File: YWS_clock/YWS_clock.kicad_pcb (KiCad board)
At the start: 2 copper layers, 140 x 90 mm, 63 parts, among them J1 Conn_01x06, J2 Power_inlet_vertical, J3 Conn_01x06, J4 Conn_02x03_Odd_Even, SW1 Omron_B3F_SPST, SW2 Omron_B3F_SPST, SW3 Omron_B3F_SPST, SW4 Omron_B3F_SPST, U1 L7805, U2 ATmega328-PU, U3 DS1307_DIP-8, U4 MAX7219, U5 MAX7219, U6 MAX7219, U7 MAX7219, Y1 Crystal_32768Hz, Y2 Crystal_16MHz

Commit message: 3 error fixed
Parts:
- removed D6: LED_0805, footprints:LED_0805_2012Metric
- removed R16: R_0805_2.2K, footprints:R_0805_2012Metric
- C1: value C_0805_10uf -> C_0805_0.1uf
- J2: value Power_inlet_vertical -> PJ-102AH; footprint footprints:Wurth-694106402002 -> footprints:PJ-102AH; moved to F.Cu
- moved C1 20.6 mm to (166.8, 120.0)
- moved J2 1.13 mm to (141.2, 137.4)
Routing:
- net Net-(U2-Pad21): track 9.40 -> 24.7 mm, vias 0 -> 2
- net Net-(C6-Pad1): track 25.6 -> 19.1 mm
- net LED_SCK: track 109.6 -> 104.4 mm
- net Net-(D6-Pad2): track 5.12 -> 0.00 mm
- net GND: track 99.0 -> 100.3 mm, vias 32 -> 31
- net RXD: track 81.7 -> 81.2 mm

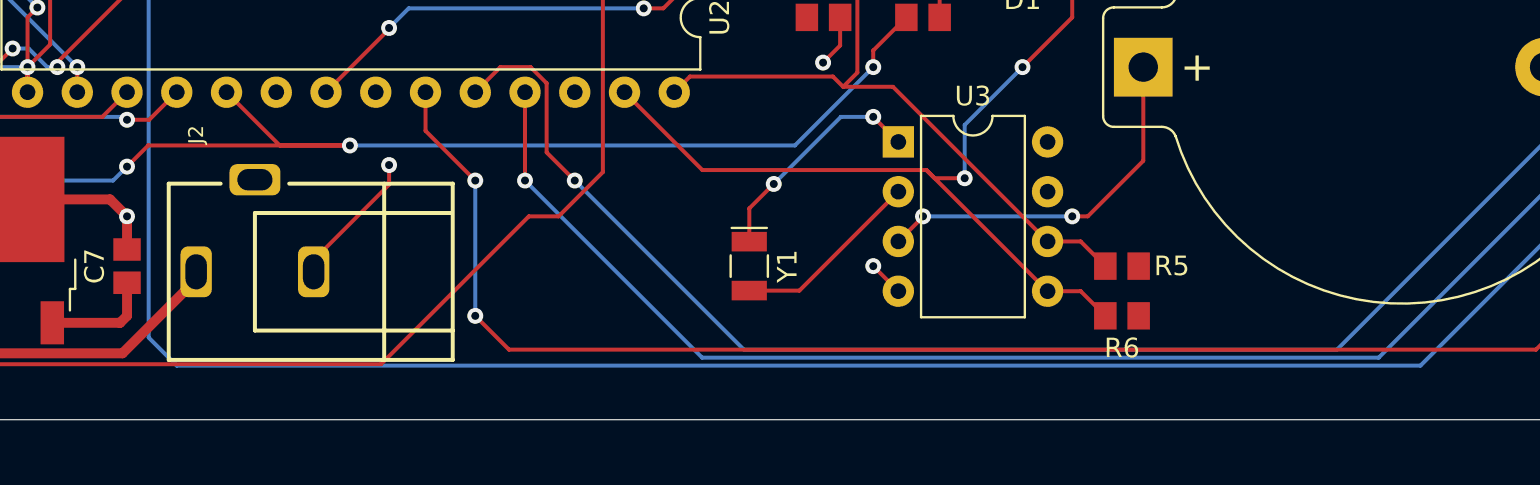
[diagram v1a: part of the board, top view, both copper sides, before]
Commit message: flip the power init
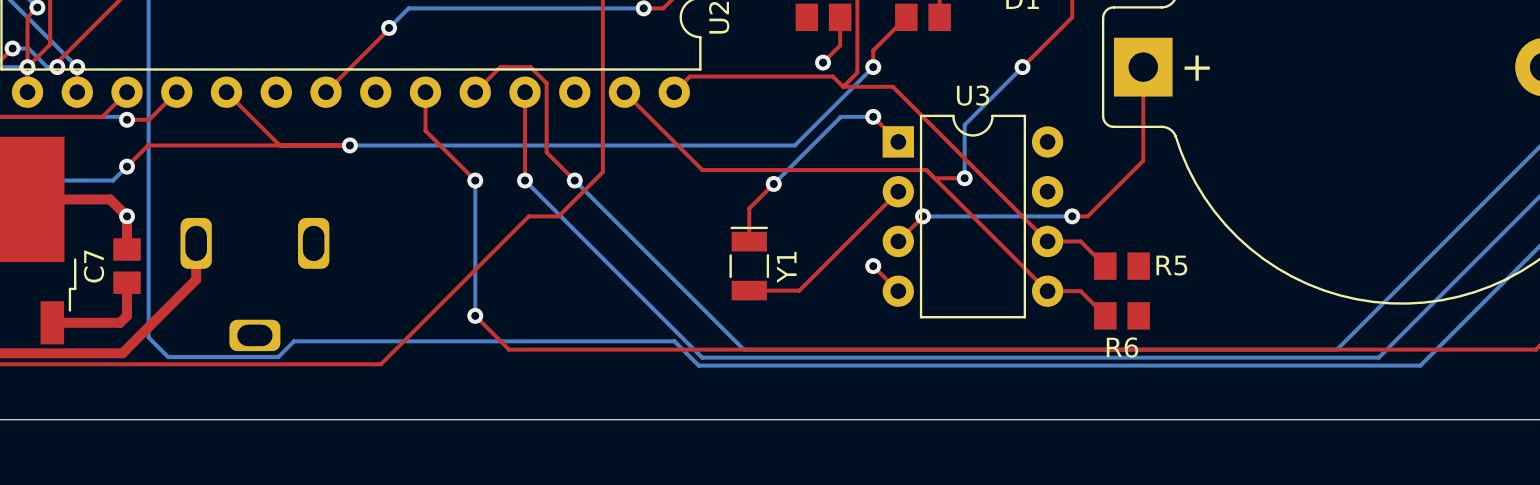
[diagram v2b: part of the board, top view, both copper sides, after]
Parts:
- J2: moved to B.Cu
- moved J2 1.45 mm to (141.2, 136.0), turned to 90 degrees
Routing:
- net GND: track 100.3 -> 93.6 mm, vias 31 -> 30
- net Net-(C6-Pad1): track 19.1 -> 21.1 mm
- net JOYST_SW: track 106.6 -> 107.3 mm
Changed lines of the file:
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@@
   (net 3 "BUZZER")
   (net 4 "VCC")
-  (net 5 "Net-(U2-Pad21)")
+  (net 5 "Net-(C1-Pad1)")
   (net 6 "Net-(C3-Pad1)")
   (net 7 "Net-(C4-Pad1)")
@@
     (fp_line (start -1 -0.6) (end 1 -0.6) (layer "F.Fab") (width 0.1))
     (pad "1" smd rect locked (at -0.85 0) (size 1.15 1.4) (layers "F.Cu" "F.Paste" "F.Mask")
-      (net 5 "Net-(U2-Pad21)") (pintype "passive"))
+      (net 5 "Net-(C1-Pad1)") (pintype "passive"))
     (pad "2" smd rect locked (at 0.85 0) (size 1.15 1.4) (layers "F.Cu" "F.Paste" "F.Mask")
       (net 1 "GND") (pintype "passive"))
@@
     )
   )
-  (footprint "footprints:PJ-102AH" (layer "F.Cu")
-    (at 141.15 137.4492 -90)
-    (descr "Power Barrel Connector Jack 2.00mm ID (0.079\"), 5.50mm OD (0.217\") Through Hole, Right Angle")
-    (property "Digikey PN" "CP-102AH-ND")
-    (property "MFG" "CUI Devices")
-    (property "MPN" "PJ-102AH")
-    (property "Mouser PN" "490-PJ-102AH")
-    (property "Sheetfile" "YWS_clock.kicad_sch")
-    (property "Sheetname" "")
-    (attr through_hole)
-    (fp_text reference "J2" (at -7 3 90) (layer "F.SilkS")
-      (effects (font (size 0.762 0.762) (thickness 0.1524)))
-    )
-    (fp_text value "PJ-102AH" (at 0 0 90) (layer "F.SilkS") hide
-      (effects (font (size 0.762 0.762) (thickness 0.1524)))
-    )
-    (fp_line (start -4.5 4.4) (end 4.5 4.4) (layer "F.SilkS") (width 0.2032))
-    (fp_line (start 3 0) (end -3 0) (layer "F.SilkS") (width 0.2032))
-    (fp_line (start -4.5 4.4) (end -4.5 1.75) (layer "F.SilkS") (width 0.2032))
-    (fp_line (start -4.5 -10.1) (end -4.5 -1.75) (layer "F.SilkS") (width 0.2032))
-    (fp_line (start -4.5 -6.6) (end 4.5 -6.6) (layer "F.SilkS") (width 0.2032))
-    (fp_line (start 4.5 4.4) (end 4.5 -10.1) (layer "F.SilkS") (width 0.2032))
-    (fp_line (start -3 0) (end -3 -10) (layer "F.SilkS") (width 0.2032))
-    (fp_line (start 4.5 -10.1) (end -4.5 -10.1) (layer "F.SilkS") (width 0.2032))
-    (fp_line (start 3 -10.1) (end 3 0) (layer "F.SilkS") (width 0.2032))
-    (pad "1" thru_hole roundrect (at 0 3 270) (size 2.6 1.6) (drill oval 1.8 1.1) (layers *.Cu *.Mask) (roundrect_rratio 0.25)
-      (net 110 "Net-(C6-Pad1)") (pinfunction "POLE") (pintype "passive"))
-    (pad "2" thru_hole roundrect (at 0 -3 270) (size 2.6 1.6) (drill oval 1.8 1.1) (layers *.Cu *.Mask) (roundrect_rratio 0.25)
-      (net 1 "GND") (pinfunction "OUT") (pintype "passive"))
-    (pad "3" thru_hole roundrect (at -4.7 0 270) (size 1.6 2.6) (drill oval 1.1 1.8) (layers *.Cu *.Mask) (roundrect_rratio 0.25)
-      (net 107 "unconnected-(J2-Pad3)") (pinfunction "OUT") (pintype "passive+no_connect"))
-    (model "${HPS3DMOD}/PJ-102A.wrl"
-      (offset (xyz 0 0 0))
-      (scale (xyz 1 1 1))
-      (rotate (xyz 0 0 0))
-    )
-  )
   (footprint "footprints:C_0805_2012Metric" (layer "F.Cu")
     (at 151.57 116.84)
@@
       (net 4 "VCC") (pinfunction "AVCC") (pintype "power_in"))
     (pad "21" thru_hole oval locked (at 7.62 17.78 270) (size 1.6 1.6) (drill 0.8) (layers *.Cu *.Mask)
-      (net 5 "Net-(U2-Pad21)") (pinfunction "AREF") (pintype "passive"))
+      (net 5 "Net-(C1-Pad1)") (pinfunction "AREF") (pintype "passive"))
     (pad "22" thru_hole oval locked (at 7.62 15.24 270) (size 1.6 1.6) (drill 0.8) (layers *.Cu *.Mask)
       (net 1 "GND") (pinfunction "GND") (pintype "power_in"))
@@
     )
   )
+  (footprint "footprints:PJ-102AH" (layer "B.Cu")
+    (at 141.15 136 90)
+    (descr "Power Barrel Connector Jack 2.00mm ID (0.079\"), 5.50mm OD (0.217\") Through Hole, Right Angle")
+    (property "Digikey PN" "CP-102AH-ND")
+    (property "MFG" "CUI Devices")
+    (property "MPN" "PJ-102AH")
+    (property "Mouser PN" "490-PJ-102AH")
+    (property "Sheetfile" "YWS_clock.kicad_sch")
+    (property "Sheetname" "")
+    (attr through_hole)
+    (fp_text reference "J2" (at -7 -3 90) (layer "B.SilkS")
+      (effects (font (size 0.762 0.762) (thickness 0.1524)) (justify mirror))
+    )
+    (fp_text value "PJ-102AH" (at 0 0 90) (layer "B.SilkS") hide
+      (effects (font (size 0.762 0.762) (thickness 0.1524)) (justify mirror))
+    )
+    (fp_line (start -4.5 -4.4) (end 4.5 -4.4) (layer "B.SilkS") (width 0.2032))
+    (fp_line (start 3 0) (end -3 0) (layer "B.SilkS") (width 0.2032))
+    (fp_line (start -4.5 -4.4) (end -4.5 -1.75) (layer "B.SilkS") (width 0.2032))
+    (fp_line (start -4.5 10.1) (end -4.5 1.75) (layer "B.SilkS") (width 0.2032))
+    (fp_line (start -4.5 6.6) (end 4.5 6.6) (layer "B.SilkS") (width 0.2032))
+    (fp_line (start 4.5 -4.4) (end 4.5 10.1) (layer "B.SilkS") (width 0.2032))
+    (fp_line (start -3 0) (end -3 10) (layer "B.SilkS") (width 0.2032))
+    (fp_line (start 4.5 10.1) (end -4.5 10.1) (layer "B.SilkS") (width 0.2032))
+    (fp_line (start 3 10.1) (end 3 0) (layer "B.SilkS") (width 0.2032))
+    (pad "1" thru_hole roundrect (at 0 -3 90) (size 2.6 1.6) (drill oval 1.8 1.1) (layers *.Cu *.Mask) (roundrect_rratio 0.25)
+      (net 110 "Net-(C6-Pad1)") (pinfunction "POLE") (pintype "passive"))
+    (pad "2" thru_hole roundrect (at 0 3 90) (size 2.6 1.6) (drill oval 1.8 1.1) (layers *.Cu *.Mask) (roundrect_rratio 0.25)
+      (net 1 "GND") (pinfunction "OUT") (pintype "passive"))
+    (pad "3" thru_hole roundrect (at -4.7 0 90) (size 1.6 2.6) (drill oval 1.1 1.8) (layers *.Cu *.Mask) (roundrect_rratio 0.25)
+      (net 107 "unconnected-(J2-Pad3)") (pinfunction "OUT") (pintype "passive+no_connect"))
+    (model "${HPS3DMOD}/PJ-102A.wrl"
+      (offset (xyz 0 0 0))
+      (scale (xyz 1 1 1))
+      (rotate (xyz 0 0 0))
+    )
+  )
   (gr_line locked (start 220 60) (end 220 140) (layer "Edge.Cuts") (width 0.05))
   (gr_line locked (start 80 60) (end 80 140) (layer "Edge.Cuts") (width 0.05))
@@
   (segment (start 134.62 136.31) (end 134.62 134.62) (width 0.508) (layer "F.Cu") (net 1))
   (segment (start 96.945 132.08) (end 96.52 132.08) (width 0.2032) (layer "F.Cu") (net 1))
-  (segment (start 144 137) (end 148 133) (width 0.2032) (layer "F.Cu") (net 1))
   (segment (start 175.55 63.21) (end 175.26 63.5) (width 0.2032) (layer "F.Cu") (net 1))
   (segment (start 95.52 120) (end 95.52 117.21) (width 0.2032) (layer "F.Cu") (net 1))
-  (segment (start 148 133) (end 148 132) (width 0.2032) (layer "F.Cu") (net 1))
   (segment (start 91.37 113.15) (end 91.37 112.61) (width 0.2032) (layer "F.Cu") (net 1))
   (segment (start 191.35 114.3) (end 193.04 114.3) (width 0.2032) (layer "F.Cu") (net 1))
@@
   (via (at 96.52 132.08) (size 0.8128) (drill 0.4064) (layers "F.Cu" "B.Cu") (net 1))
   (via (at 121.92 134.62) (size 0.8128) (drill 0.4064) (layers "F.Cu" "B.Cu") (net 1))
-  (via (at 148 132) (size 0.8128) (drill 0.4064) (layers "F.Cu" "B.Cu") (net 1))
   (via (at 142.24 63.5) (size 0.8128) (drill 0.4064) (layers "F.Cu" "B.Cu") (net 1))
   (via (at 165.1 111.76) (size 0.8128) (drill 0.4064) (layers "F.Cu" "B.Cu") (net 1))
@@
   (via (at 134.62 121.92) (size 0.8128) (drill 0.4064) (layers "F.Cu" "B.Cu") (net 80))
   (via (at 213.36 129.54) (size 0.8128) (drill 0.4064) (layers "F.Cu" "B.Cu") (net 80))
-  (segment (start 137.16 142.24) (end 135.724311 140.804311) (width 0.2032) (layer "B.Cu") (net 80))
-  (segment (start 135.724311 123.024311) (end 134.62 121.92) (width 0.2032) (layer "B.Cu") (net 80))
+  (segment (start 162.575242 141) (end 143.146058 141) (width 0.2032) (layer "B.Cu") (net 80))
   (segment (start 213.36 129.54) (end 200.66 142.24) (width 0.2032) (layer "B.Cu") (net 80))
-  (segment (start 200.66 142.24) (end 137.16 142.24) (width 0.2032) (layer "B.Cu") (net 80))
   (segment (start 135.724311 140.804311) (end 135.724311 123.024311) (width 0.2032) (layer "B.Cu") (net 80))
+  (segment (start 142.341738 141.80432) (end 136.72432 141.80432) (width 0.2032) (layer "B.Cu") (net 80))
+  (segment (start 163.815242 142.24) (end 162.575242 141) (width 0.2032) (layer "B.Cu") (net 80))
+  (segment (start 135.724311 123.024311) (end 134.62 121.92) (width 0.2032) (layer "B.Cu") (net 80))
+  (segment (start 136.72432 141.80432) (end 135.724311 140.804311) (width 0.2032) (layer "B.Cu") (net 80))
+  (segment (start 143.146058 141) (end 142.341738 141.80432) (width 0.2032) (layer "B.Cu") (net 80))
+  (segment (start 200.66 142.24) (end 163.815242 142.24) (width 0.2032) (layer "B.Cu") (net 80))
   (segment (start 174.41 124.46) (end 172.72 126.15) (width 0.2032) (layer "F.Cu") (net 82))
   (segment (start 135.7 131) (end 134.62 132.08) (width 0.2032) (layer "F.Cu") (net 82))
@@
   (segment (start 172.72 107.673267) (end 178.793267 101.6) (width 0.2032) (layer "B.Cu") (net 106))
   (segment (start 178.793267 101.6) (end 180.34 101.6) (width 0.2032) (layer "B.Cu") (net 106))
-  (segment (start 134.388289 141.611711) (end 138 138) (width 0.508) (layer "F.Cu") (net 110))
-  (segment (start 124.2 138.01) (end 126.245 140.055) (width 0.508) (layer "F.Cu") (net 110))
-  (segment (start 127.801711 141.611711) (end 134.388289 141.611711) (width 0.508) (layer "F.Cu") (net 110))
   (segment (start 126.245 140.055) (end 127.801711 141.611711) (width 0.508) (layer "F.Cu") (net 110))
+  (segment (start 127.801711 141.611711) (end 134.388289 141.611711) (width 0.508) (layer "F.Cu") (net 110))
+  (segment (start 138.15 137.85) (end 138.15 136) (width 0.508) (layer "F.Cu") (net 110))
+  (segment (start 124.2 138.01) (end 126.245 140.055) (width 0.508) (layer "F.Cu") (net 110))
+  (segment (start 134.388289 141.611711) (end 138.15 137.85) (width 0.508) (layer "F.Cu") (net 110))
   (segment (start 121.92 138.01) (end 124.2 138.01) (width 0.508) (layer "F.Cu") (net 110))
   (segment (start 117.15 131.69) (end 114.22 134.62) (width 0.2032) (layer "F.Cu") (net 111))
